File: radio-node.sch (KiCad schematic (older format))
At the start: 39 parts

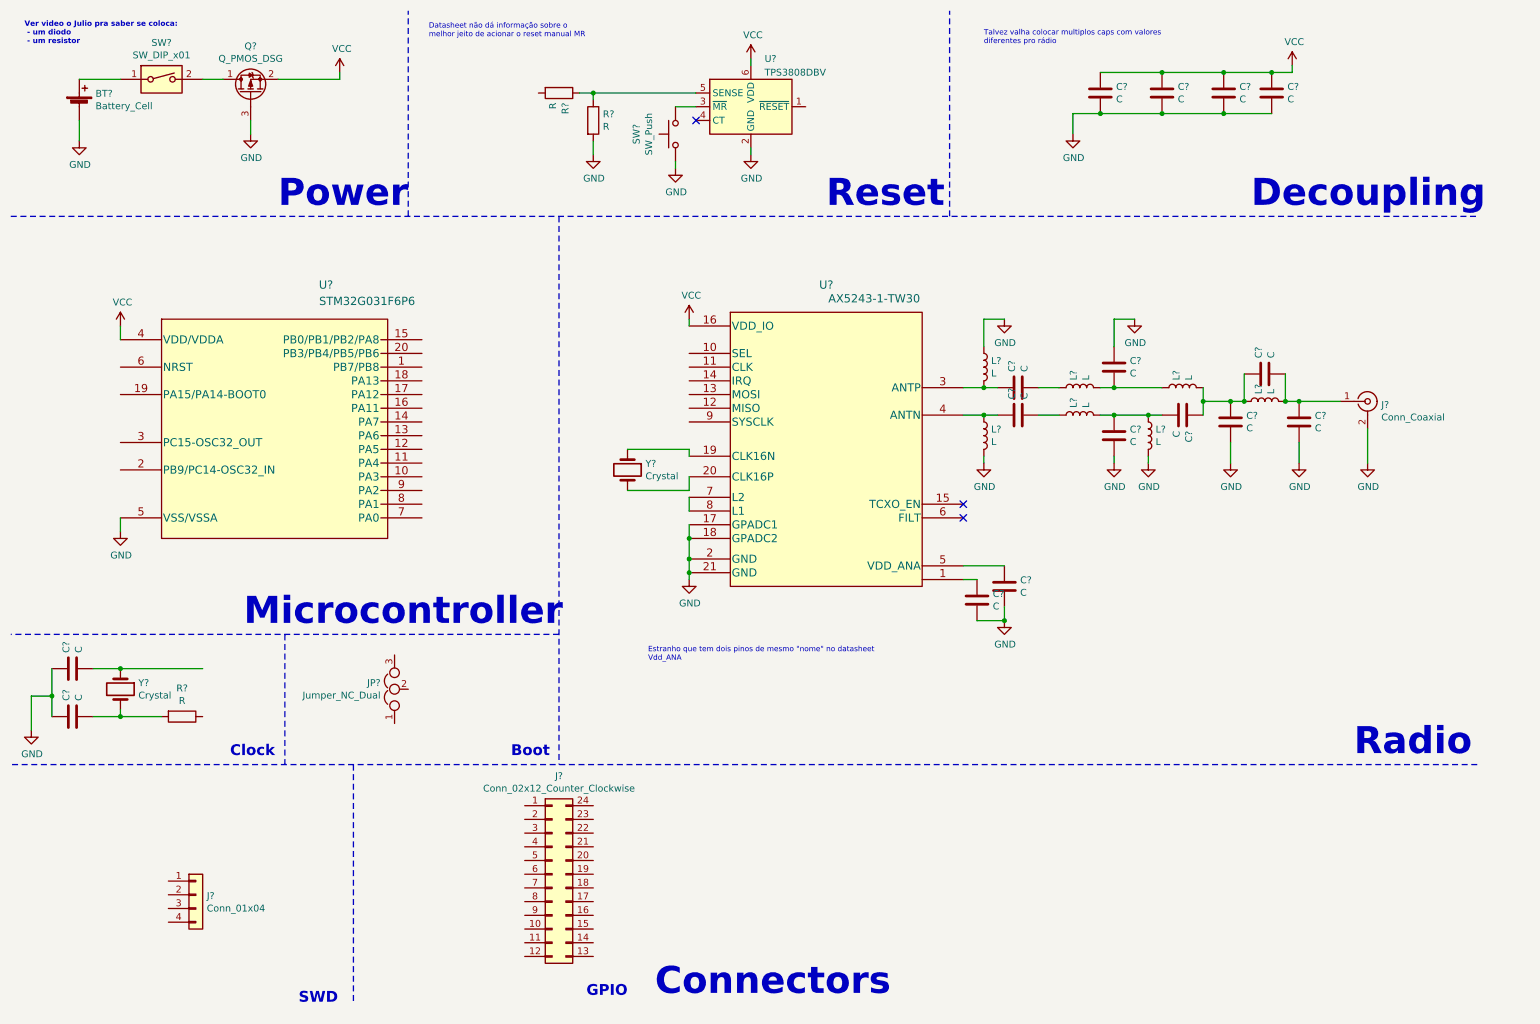
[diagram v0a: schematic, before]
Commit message: Fully Connected schematic
Signed-off-by: Leonardo Celente <leocelente@gmail.com>
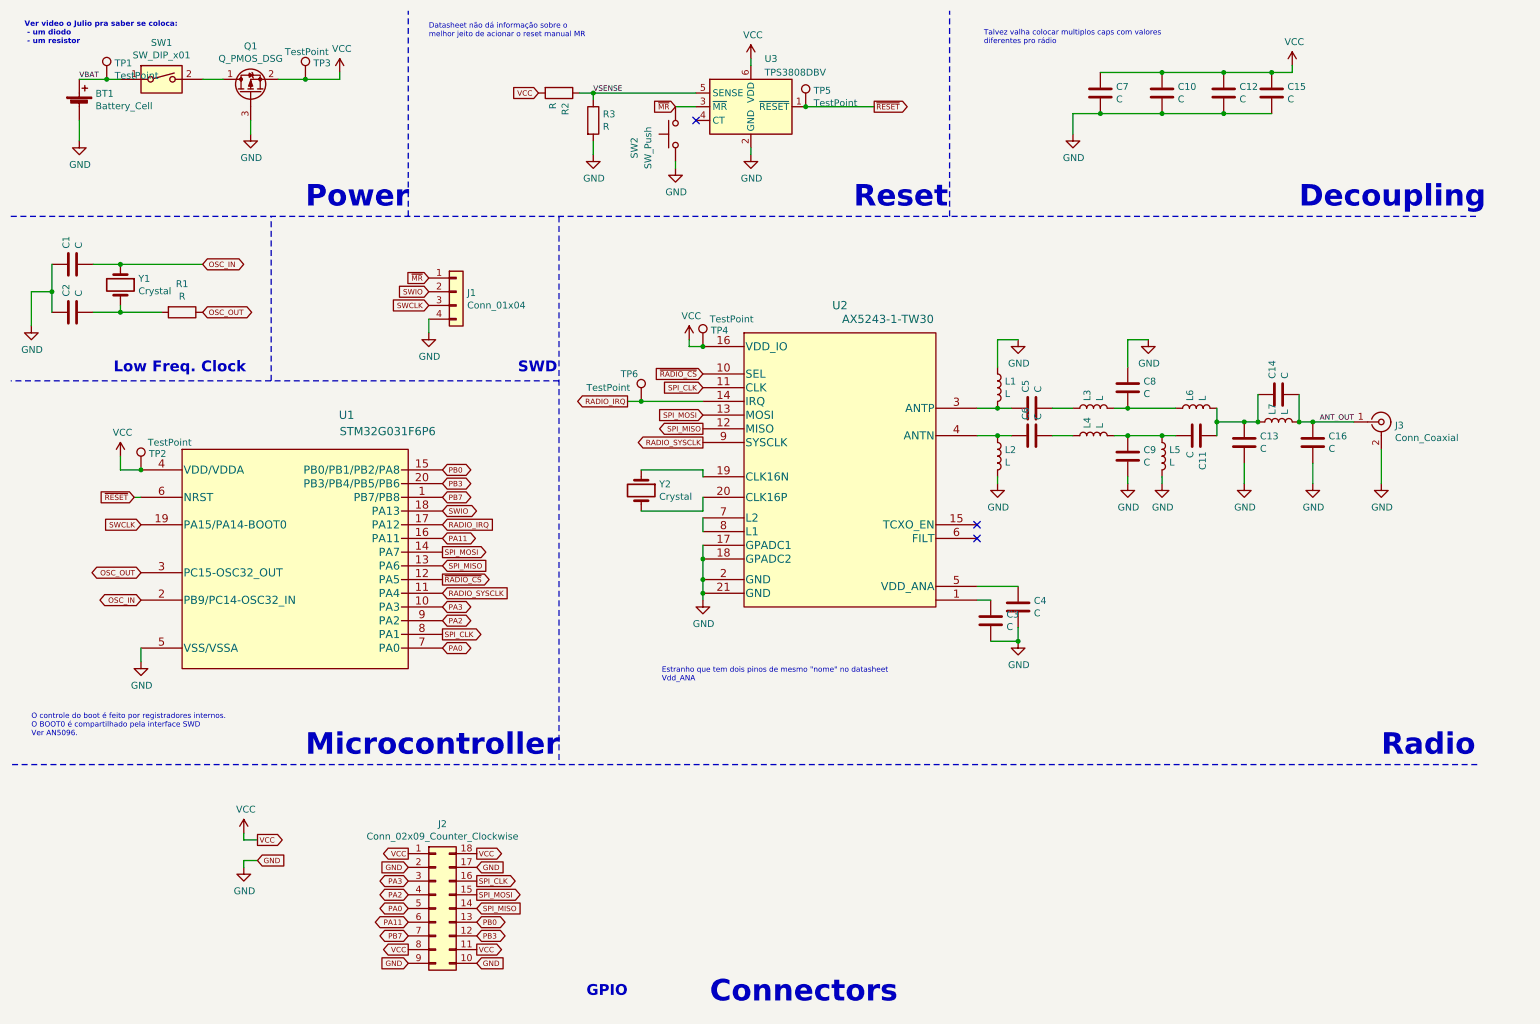
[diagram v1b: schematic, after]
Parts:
- removed J?: Conn_02x12_Counter_Clockwise, symbol Connector_Generic:Conn_02x12_Counter_Clockwise
- removed JP?: Jumper_NC_Dual, symbol Device:Jumper_NC_Dual
- added J2: Conn_02x09_Counter_Clockwise, symbol Connector_Generic:Conn_02x09_Counter_Clockwise
- added TP1, TP2, TP3, TP4, TP5, TP6: TestPoint, symbol Connector:TestPoint
- gave numbers to parts that had none: 37
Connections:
- net GND: now also J1.4 (Pin_4), J2.10 (Pin_10), J2.17 (Pin_17), J2.2 (Pin_2), J2.9 (Pin_9)
- net VCC: now also R2.2, J2.1 (Pin_1), J2.11 (Pin_11), J2.18 (Pin_18), J2.8 (Pin_8), TP2.1, TP3.1, TP4.1
- net VBAT: now reaches BT1.1 (+), SW1.1
- net VBAT: now also TP1.1
- net PB7: now reaches U1.1 (PB7/PB8)
- net PB7: now also J2.7 (Pin_7)
- net PA3: now reaches U1.10 (PA3)
- net PA3: now also J2.3 (Pin_3)
- net RADIO_SYSCLK: now reaches U1.11 (PA4)
- net RADIO_SYSCLK: now also U2.9 (SYSCLK)
- net ~RADIO_CS: now reaches U1.12 (PA5)
- net ~RADIO_CS: now also U2.10 (SEL)
- net SPI_MISO: now reaches U1.13 (PA6)
- net SPI_MISO: now also U2.12 (MISO), J2.14 (Pin_14)
- net SPI_MOSI: now reaches U1.14 (PA7)
- net SPI_MOSI: now also U2.13 (MOSI), J2.15 (Pin_15)
- net PB0: now reaches U1.15 (PB0/PB1/PB2/PA8)
- net PB0: now also J2.13 (Pin_13)
- net PA11: now reaches U1.16 (PA11)
- net PA11: now also J2.6 (Pin_6)
- net RADIO_IRQ: now reaches U1.17 (PA12)
- net RADIO_IRQ: now also U2.14 (IRQ), TP6.1
- net SWIO: now reaches U1.18 (PA13)
- net SWIO: now also J1.2 (Pin_2)
- net SWCLK: now reaches U1.19 (PA15/PA14-BOOT0)
- net SWCLK: now also J1.3 (Pin_3)
- net OSC_IN: now reaches U1.2 (PB9/PC14-OSC32_IN)
- net OSC_IN: now also C1.2, Y1.1
- net PB3: now reaches U1.20 (PB3/PB4/PB5/PB6)
- net PB3: now also J2.12 (Pin_12)
- net OSC_OUT: now reaches U1.3 (PC15-OSC32_OUT)
- net OSC_OUT: now also R1.1
- net ~RESET: now reaches U1.6 (NRST)
- net ~RESET: now also U3.1 (~RESET), TP5.1
- net PA0: now reaches U1.7 (PA0)
- net PA0: now also J2.5 (Pin_5)
- net SPI_CLK: now reaches U1.8 (PA1)
- net SPI_CLK: now also U2.11 (CLK), J2.16 (Pin_16)
- net PA2: now reaches U1.9 (PA2)
- net PA2: now also J2.4 (Pin_4)
- net ANT_OUT: now reaches C14.2, C16.1, J3.1 (In), L7.2
- net ~MR: now reaches SW2.2, U3.3 (~MR)
- net ~MR: now also J1.1 (Pin_1)
- net VSENSE: now reaches R2.1, R3.1, U3.5 (SENSE)
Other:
- note added: "Low Freq. Clock"
- note added: "O controle do boot é feito por registradores internos. \nO BOOT0 é compartilhado pela interface SWD\nVer AN5096."
- note removed: "Boot"
- note removed: "Clock"
- moved on the sheet: C1, C11, C13, C14, C16, C2, C3, C4, C5, C6, C8, C9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
